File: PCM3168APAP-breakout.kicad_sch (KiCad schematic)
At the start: 31 parts, among them IC101 PCM3168APAP, IC102 SN74LVC2G34DRLR, J101 I^{2}S, J102 I^{2}C, J103 MISC, J104 DOUT

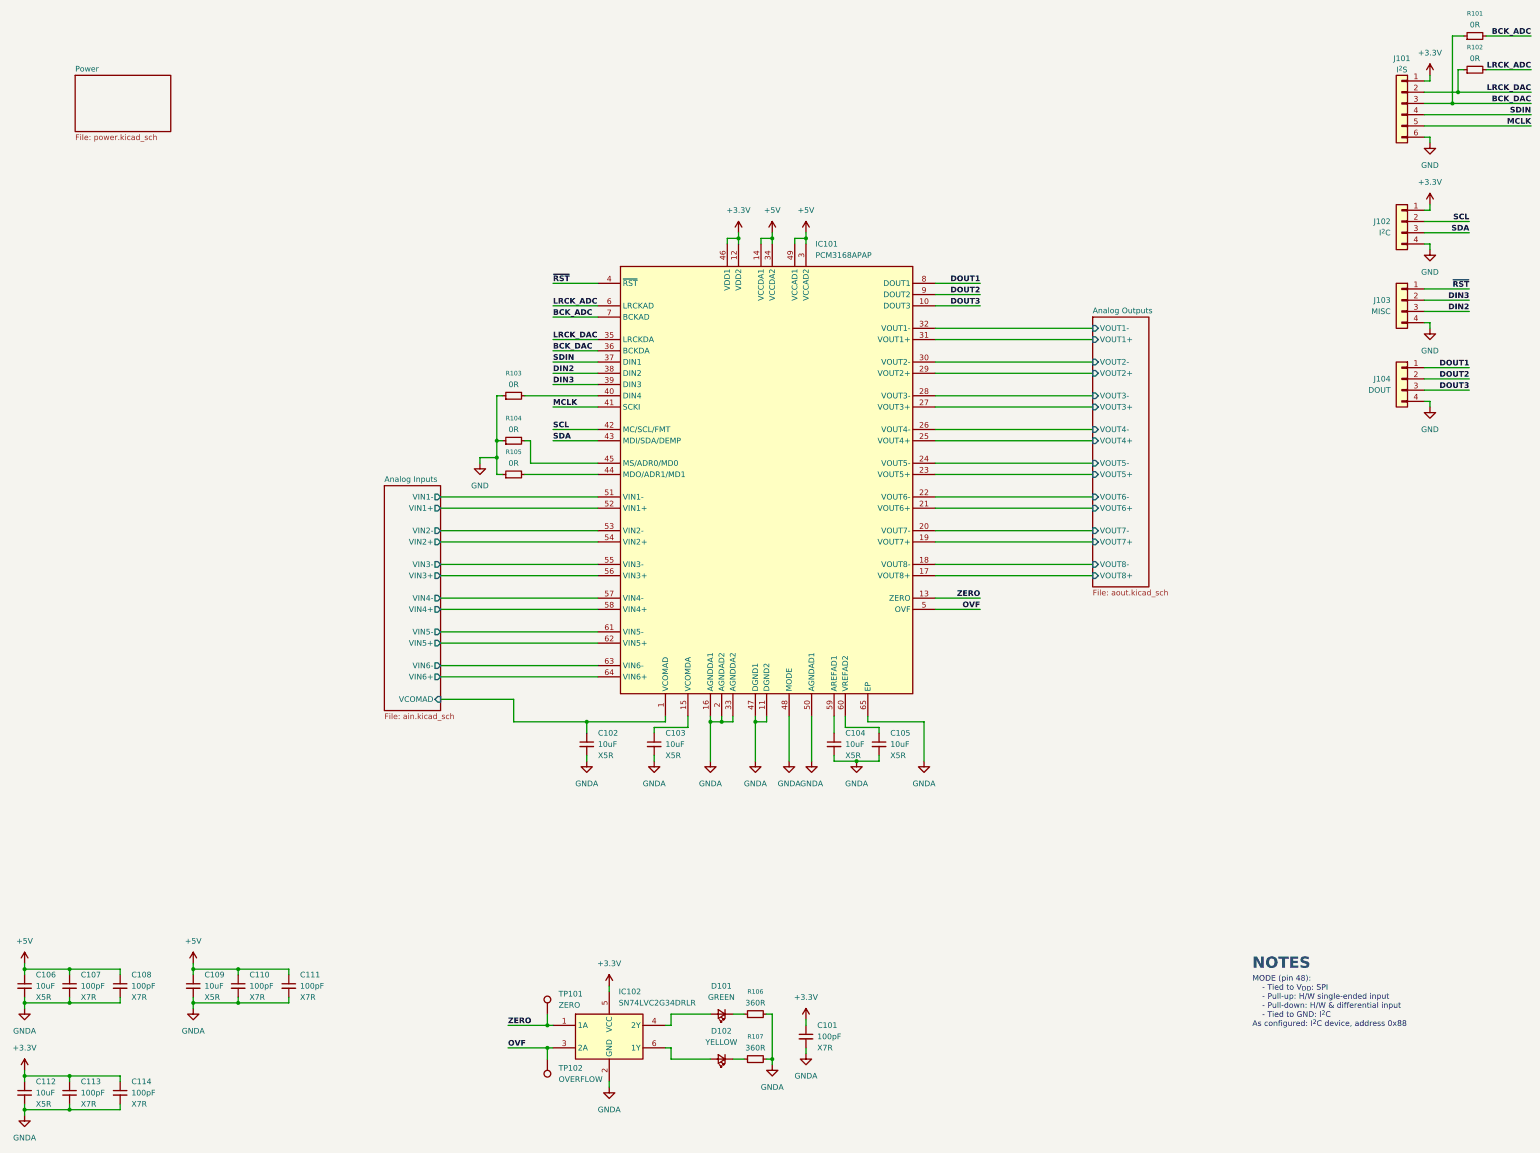
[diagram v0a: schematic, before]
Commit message: Cleaned up schematic
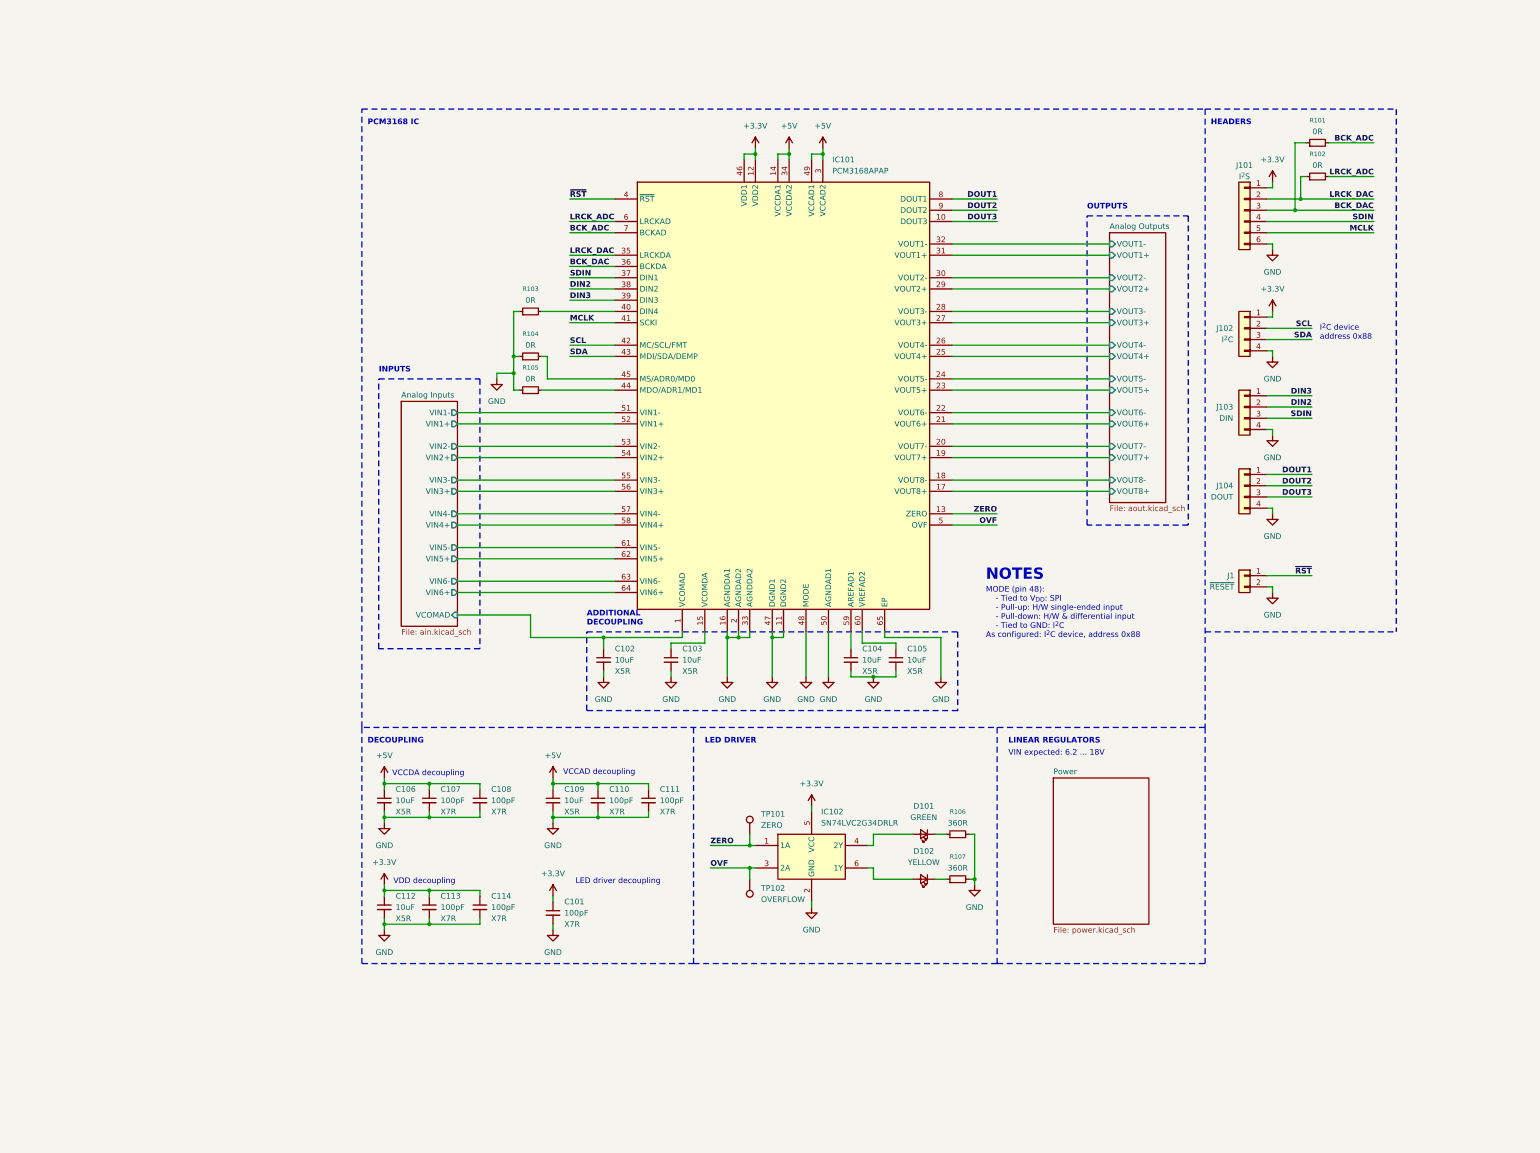
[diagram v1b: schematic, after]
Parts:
- added J1: ~{RESET}, Connector_PinHeader_2.54mm:PinHeader_1x02_P2.54mm_Vertical, symbol Connector_Generic:Conn_01x02
- J103: value MISC -> DIN
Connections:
- net GNDA is gone; now on net GND: C101.2, C102.2, C103.2, C104.2, C105.2, C106.2, C107.2, C108.2, C109.2, C110.2, C111.2, C112.2, C113.2, C114.2, IC101.11 (DGND2), IC101.16 (AGNDDA1), IC101.2 (AGNDAD2), IC101.33 (AGNDDA2), IC101.47 (DGND1), IC101.48 (MODE), IC101.50 (AGNDAD1), IC101.65 (EP), IC102.2 (GND), R106.2, R107.2
- net DIN2: now also J103.2 (Pin_2); no longer J103.3 (Pin_3)
- net DIN3: now also J103.1 (Pin_1); no longer J103.2 (Pin_2)
- net GND: now also J1.2 (Pin_2)
- net SDIN: now also J103.3 (Pin_3)
- net ~{RST}: now also J1.1 (Pin_1); no longer J103.1 (Pin_1)
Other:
- note added: "ADDITIONAL DECOUPLING"
- note added: "DECOUPLING"
- note added: "HEADERS"
- note added: "INPUTS"
- note added: "I^{2}C device address 0x88"
- note added: "LED DRIVER"
- note added: "LED driver decoupling"
- note added: "LINEAR REGULATORS"
- note added: "OUTPUTS"
- note added: "PCM3168 IC"
- note added: "VCCAD decoupling"
- note added: "VCCDA decoupling"
- note added: "VDD decoupling"
- note added: "VIN expected: 6.2 ... 18V"
- moved on the sheet: C101, C102, C103, C104, C105, C106, C107, C108, C109, C110, C111, C112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
